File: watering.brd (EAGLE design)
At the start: 84.8 x 54.6 mm, 36 parts, among them IC1 LM324N, IC2 7805T, J1 DCJ0202, Q1 IRF510, T1 2N2222, T2 2N2222, T3 2N2222A

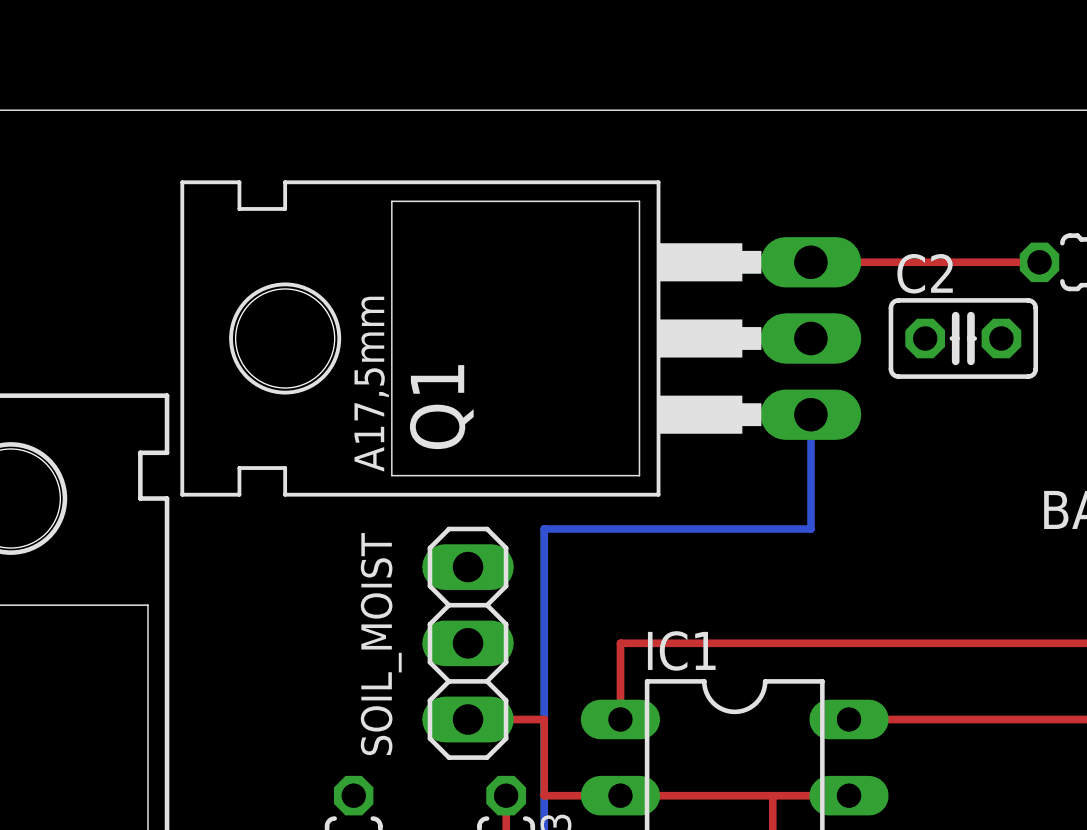
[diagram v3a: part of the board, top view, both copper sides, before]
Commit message: Add pull-down resistor for MOSFET and changed MOSFET type to IRLZ44N
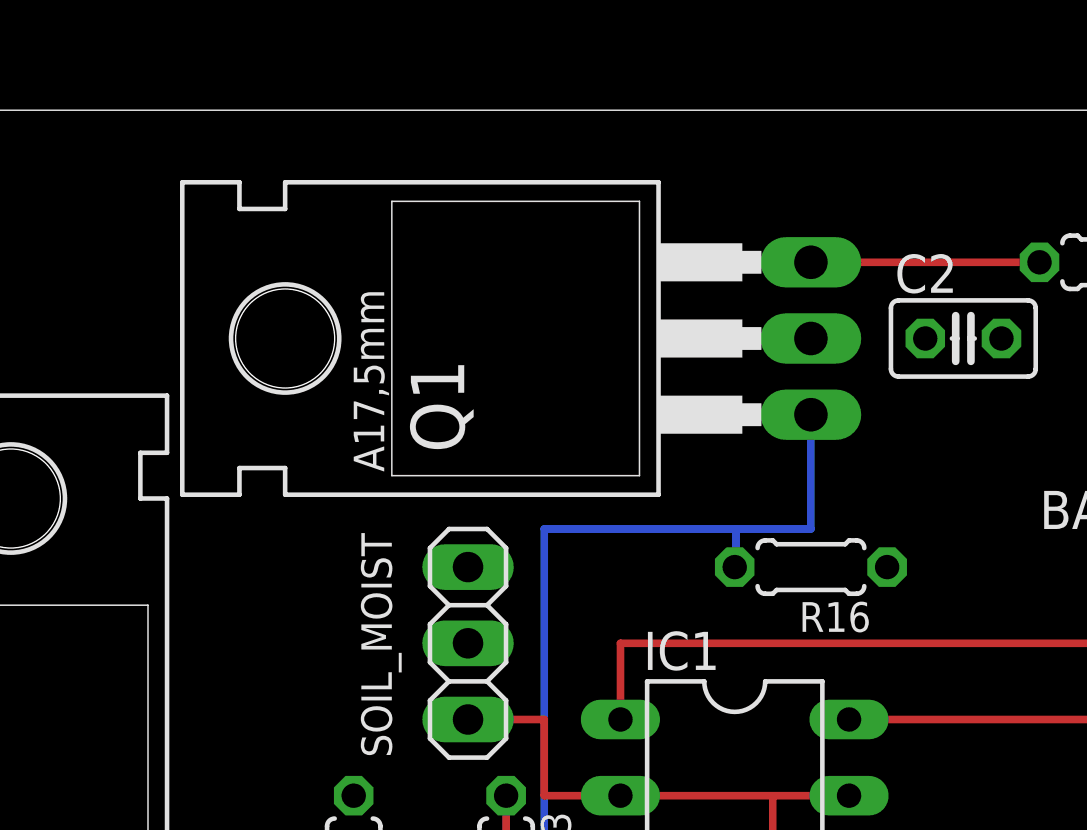
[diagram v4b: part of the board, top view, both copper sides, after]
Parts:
- added R16: 10k, resistor:0204/5
- Q1: value IRF510 -> IRLZ44Z; device transistor-fet:TO220 -> transistor-power:TO220BH
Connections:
- net +5V: now also Q1.D; no longer Q1.2
- net GND: now also R16.1
- net N$7: now also Q1.G, R16.2; no longer Q1.1
- net N$8: now also Q1.S; no longer Q1.3
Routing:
- net N$7: track 36.8 -> 38.1 mm
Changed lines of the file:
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@@
 </class>
 </classes>
-<designrules name="default">
+<designrules name="default *">
 <description language="de">&lt;b&gt;EAGLE Design Rules&lt;/b&gt;
 &lt;p&gt;
@@
 <element name="R6" library="resistor" package="0204/5" value="1k" x="17.78" y="21.59" rot="R270"/>
 <element name="R7" library="resistor" package="0204/5" value="10k" x="22.86" y="21.59" rot="R90"/>
-<element name="Q1" library="transistor-fet" package="TO220" value="IRF510" x="26.67" y="46.99" rot="R90"/>
+<element name="Q1" library="transistor-power" package="TO220BH" value="IRLZ44Z" x="26.67" y="46.99" rot="R90"/>
 <element name="R8" library="resistor" package="0204/5" value="220" x="43.18" y="49.53" rot="R180"/>
 <element name="BATTERY" library="led" package="LED3MM" value="" x="44.45" y="44.45" smashed="yes" rot="R180">
@@
 <element name="JP1" library="pinhead" package="1X01" value="JP2_DSIG" x="76.2" y="19.05" smashed="yes" rot="R90"/>
 <element name="R15" library="resistor" package="0204/5" value="4.7k" x="78.74" y="16.51" rot="R90"/>
+<element name="R16" library="resistor" package="0204/5" value="10k" x="33.02" y="39.37" rot="R180"/>
 </elements>
 <signals>
@@
 <vertex x="-2.54" y="0"/>
 </polygon>
+<contactref element="R16" pad="1"/>
 </signal>
 <signal name="SOIL_IN">
@@
 <contactref element="T2" pad="3"/>
 <contactref element="T3" pad="3"/>
-<contactref element="Q1" pad="2"/>
+<contactref element="Q1" pad="D"/>
 <contactref element="R2" pad="2"/>
 <polygon width="0.254" layer="16" isolate="0.3048">
@@
 <signal name="N$7">
 <contactref element="IC1" pad="7"/>
-<contactref element="Q1" pad="1"/>
+<contactref element="Q1" pad="G"/>
 <wire x1="26.67" y1="19.05" x2="24.13" y2="19.05" width="0.254" layer="16"/>
 <wire x1="24.13" y1="19.05" x2="24.13" y2="40.64" width="0.254" layer="16"/>
-<wire x1="24.13" y1="40.64" x2="33.02" y2="40.64" width="0.254" layer="16"/>
+<wire x1="30.523034375" y1="40.64" x2="24.13" y2="40.64" width="0.254" layer="16"/>
+<wire x1="30.523034375" y1="40.64" x2="33.02" y2="40.64" width="0.254" layer="16"/>
 <wire x1="33.02" y1="40.64" x2="33.02" y2="44.45" width="0.254" layer="16"/>
+<contactref element="R16" pad="2"/>
+<wire x1="30.48" y1="39.37" x2="30.523034375" y2="39.37" width="0.254" layer="16"/>
+<wire x1="30.523034375" y1="39.37" x2="30.523034375" y2="40.64" width="0.254" layer="16"/>
 </signal>
 <signal name="N$8">
-<contactref element="Q1" pad="3"/>
+<contactref element="Q1" pad="S"/>
 <contactref element="R8" pad="2"/>
 <wire x1="33.02" y1="49.53" x2="40.64" y2="49.53" width="0.254" layer="1"/>
